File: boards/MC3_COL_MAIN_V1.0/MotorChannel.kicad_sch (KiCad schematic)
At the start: 7 parts, among them J7 MOTOR, U3 DRV8214RTER

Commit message: Schematic: local VM bulk per channel + LDO input filter
Two changes to isolate motor switching noise from the +3V3 rail.

1. MotorChannel.kicad_sch gains a 10 uF 0805 (C15850) from VM to GND beside
   the existing 1 uF. One symbol in the shared sheet, so five caps on the
   board. TI asks for 0.1 uF plus bulk at VM and the board bulk was over in
   the power block, at the far end of the VM trunk.

2. Power.kicad_sch gains FB4 + C32 on a new VM_LDO net between VM and the
   AMS1117's VI pin, plus a PWR_FLAG the new net needs for ERC. The regulator
   was a direct path from the motor rail to +3V3 - its PSRR is down to about
   30 dB by 100 kHz, well inside the PWM band.

FB4 is C14709 (Murata BLM18PG121SN1D, 120R@100MHz, 2 A, 50 mohm), NOT the 600R
C1002 used on VDDA and VCAN5 - that part is 200 mA / 450 mohm and would have
been marginal on current and cost ~110 mV of the AMS1117's dropout headroom.

Flagged in MIGRATION: FB4 with C32 forms an LC at roughly 115 kHz with Q ~2.8,
which could amplify rather than attenuate if the motor PWM lands near it. Needs
the firmware's PWM frequency to close, and damping (tantalum or an R leg) if it
does - shrinking C32 would make it worse, not better.

ERC: 0 errors, the same 8 intentional same_local_global warnings as before.

Co-Authored-By: Claude Opus 5 (1M context) <noreply@anthropic.com>
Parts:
- added C31: 10uF, MC3_COL_MAIN:C_0805_2012Metric, symbol Device:C
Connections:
- net GND: now also C31.2
- net VM: now also C31.1
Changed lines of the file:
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@@
 	(generator_version "10.0")
 	(paper "A4")
-	(text "Motor channel - one per leaf, instantiated x4. Implements: COL-COTS-0028 (DRV8214, integrated current sense + ripple counting) - vault Main-Board-01 Motor Channel. Layout: docs/design/parts/DRV8214.md. PAD + GND to the GND plane via thermal vias. VREF = +3V3 (TI typical app). PROVISIONAL: R_IPROPI, pull-ups."
-		(exclude_from_sim no)
-		(at 40 30 0)
-		(effects
-			(font
-				(size 1.5 1.5)
-			)
-		)
-	)
-	(text "Review 2026-08-22: R_IPROPI 6.8k -> hardware current trip 1.99 A (was 8.45k -> 1.60 A)."
-		(exclude_from_sim no)
-		(at 40 120 0)
-		(effects
-			(font
-				(size 1.5 1.5)
-			)
-		)
-	)
-	(text "A1/A0 tri-level address straps are set per instance on the root sheet (GND / +3V3)."
-		(exclude_from_sim no)
-		(at 40 115 0)
-		(effects
-			(font
-				(size 1.5 1.5)
-			)
-		)
-	)
 	(wire
 		(pts
-			(xy 87.63 82.55) (xy 85.09 82.55)
+			(xy 87.63 82.55)
+			(xy 85.09 82.55)
 		)
 		(stroke
@@
 	(wire
 		(pts
-			(xy 97.79 64.77) (xy 97.79 62.23)
+			(xy 97.79 64.77)
+			(xy 97.79 62.23)
 		)
 		(stroke
@@
 	(wire
 		(pts
-			(xy 87.63 80.01) (xy 85.09 80.01)
+			(xy 87.63 80.01)
+			(xy 85.09 80.01)
 		)
 		(stroke
@@
 	(wire
 		(pts
-			(xy 87.63 77.47) (xy 85.09 77.47)
+			(xy 87.63 77.47)
+			(xy 85.09 77.47)
 		)
 		(stroke
@@
 		)
 	)
+	(text "Motor channel - one per leaf, instantiated x4. Implements: COL-COTS-0028 (DRV8214, integrated current sense + ripple counting) - vault Main-Board-01 Motor Channel. Layout: docs/design/parts/DRV8214.md. PAD + GND to the GND plane via thermal vias. VREF = +3V3 (TI typical app). PROVISIONAL: R_IPROPI, pull-ups."
+		(at 40 30 0)
+		(effects
+			(font
+				(size 1.5 1.5)
+			)
+		)
+	)
+	(text "Review 2026-08-22: R_IPROPI 6.8k -> hardware current trip 1.99 A (was 8.45k -> 1.60 A)."
+		(at 40 120 0)
+		(effects
+			(font
+				(size 1.5 1.5)
+			)
+		)
+	)
+	(text "A1/A0 tri-level address straps are set per instance on the root sheet (GND / +3V3)."
+		(at 40 115 0)
+		(effects
+			(font
+				(size 1.5 1.5)
+			)
+		)
+	)
 	(label "+3V3"
 		(at 119.38 54.61 0)
@@
 	(label "+3V3"
 		(at 134.62 60.96 0)
+		(effects
+			(font
+				(size 1.27 1.27)
+			)
+			(justify left bottom)
+		)
+	)
+	(label "VM"
+		(at 90.17 54.61 0)
+		(effects
+			(font
+				(size 1.27 1.27)
+			)
+			(justify left bottom)
+		)
+	)
+	(label "GND"
+		(at 90.17 62.23 0)
 		(effects
 			(font
@@
 		(at 134.62 64.77 0)
 		(unit 1)
-		(body_style 1)
 		(exclude_from_sim no)
 		(in_bom yes)
 		(on_board yes)
-		(in_pos_files yes)
 		(dnp no)
 		(property "Reference" "R17"
@@
 			)
 		)
+		(body_style 1)
+		(in_pos_files yes)
 		(pin "1"
 		)
@@
 		(at 144.78 64.77 0)
 		(unit 1)
-		(body_style 1)
 		(exclude_from_sim no)
 		(in_bom yes)
 		(on_board yes)
-		(in_pos_files yes)
 		(dnp no)
 		(property "Reference" "R18"
@@
 			)
 		)
+		(body_style 1)
+		(in_pos_files yes)
 		(pin "1"
 		)
@@
 		(at 124.46 91.44 0)
 		(unit 1)
-		(body_style 1)
 		(exclude_from_sim no)
 		(in_bom yes)
 		(on_board yes)
-		(in_pos_files yes)
 		(dnp no)
 		(property "Reference" "R16"
@@
 			)
 		)
+		(body_style 1)
+		(in_pos_files yes)
 		(pin "2"
 		)
@@
 		(at 97.79 95.25 0)
 		(unit 1)
-		(body_style 1)
 		(exclude_from_sim no)
 		(in_bom yes)
 		(on_board yes)
-		(in_pos_files yes)
 		(dnp no)
 		(property "Reference" "#PWR011"
@@
 			)
 		)
+		(body_style 1)
+		(in_pos_files yes)
 		(pin "1"
 		)
@@
 		(at 80.01 58.42 0)
 		(unit 1)
-		(body_style 1)
 		(exclude_from_sim no)
 		(in_bom yes)
 		(on_board yes)
-		(in_pos_files yes)
 		(dnp no)
 		(property "Reference" "C18"
@@
 			)
 		)
+		(body_style 1)
+		(in_pos_files yes)
 		(pin "2"
 		)
@@
 		(at 100.33 80.01 0)
 		(unit 1)
-		(body_style 1)
 		(exclude_from_sim no)
 		(in_bom yes)
 		(on_board yes)
-		(in_pos_files yes)
 		(dnp no)
 		(property "Reference" "U3"
@@
 			)
 		)
+		(body_style 1)
+		(in_pos_files yes)
 		(pin "13"
 		)
@@
 		(at 149.86 95.25 0)
 		(unit 1)
-		(body_style 1)
 		(exclude_from_sim no)
 		(in_bom yes)
 		(on_board yes)
-		(in_pos_files yes)
 		(dnp no)
 		(property "Reference" "J7"
@@
 			)
 		)
+		(body_style 1)
+		(in_pos_files yes)
 		(pin "2"
 		)
@@
 		(at 102.87 64.77 0)
 		(unit 1)
-		(body_style 1)
 		(exclude_from_sim no)
 		(in_bom yes)
 		(on_board yes)
-		(in_pos_files yes)
 		(dnp no)
 		(property "Reference" "#PWR012"
@@
 			)
 		)
+		(body_style 1)
+		(in_pos_files yes)
 		(pin "1"
 		)
@@
 		(at 119.38 58.42 0)
 		(unit 1)
-		(body_style 1)
 		(exclude_from_sim no)
 		(in_bom yes)
 		(on_board yes)
-		(in_pos_files yes)
 		(dnp no)
 		(property "Reference" "C19"
@@
 			)
 		)
+		(body_style 1)
+		(in_pos_files yes)
 		(pin "1"
 		)
@@
 		)
 	)
+	(symbol
+		(lib_id "Device:C")
+		(at 90.17 58.42 0)
+		(unit 1)
+		(in_bom yes)
+		(on_board yes)
+		(dnp no)
+		(property "Reference" "C31"
+			(at 90.805 55.88 0)
+			(effects
+				(font
+					(size 1.27 1.27)
+				)
+				(justify left)
+			)
+		)
+		(property "Value" "10uF"
+			(at 90.805 60.96 0)
+			(effects
+				(font
+					(size 1.27 1.27)
+				)
+				(justify left)
+			)
+		)
+		(property "Footprint" "MC3_COL_MAIN:C_0805_2012Metric"
+			(at 90.17 58.42 0)
+			(hide yes)
+			(effects
+				(font
+					(size 1.27 1.27)
+				)
+			)
+		)
+		(property "Datasheet" ""
+			(at 90.17 58.42 0)
+			(hide yes)
+			(effects
+				(font
+					(size 1.27 1.27)
+				)
+			)
+		)
+		(instances
+			(project "MC3_COL_MAIN_V1.0"
+				(path "/7d5f4202-d55e-4c7b-a2df-dd599db38e48/5db6fbb9-0012-419b-b34a-9d86ac1f5217"
+					(reference "C31")
+					(unit 1)
+				)
+			)
+		)
+		(property "LCSC" "C15850"
+			(at 90.17 58.42 0)
+			(hide yes)
+			(effects
+				(font
+					(size 1.27 1.27)
+				)
+			)
+		)
+		(property "MPN" "CL21A106KAYNNNE"
+			(at 90.17 58.42 0)
+			(hide yes)
+			(effects
+				(font
+					(size 1.27 1.27)
+				)
+			)
+		)
+		(property "Note" "Local VM bulk, one per channel. Added 2026-08-22: TI SLVSH04 asks for 0.1uF + bulk at VM; the board bulk (C3/C4) is in the power block, so the five bridges' di/dt was being supplied through the VM trunk inductance. 25V X5R keeps most of its value at the 5V rail. PROVISIONAL - value not set by a vault CALC"
+			(at 90.17 58.42 0)
+			(hide yes)
+			(effects
+				(font
+					(size 1.27 1.27)
+				)
+			)
+		))
 )

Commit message: Schematic: new channel cap goes in as C? so annotation can assign per-instance refs
Adding it as C31 put that string in the symbol-level Reference property, so all
five sheet instances fell back to it and eeschema reported four duplicates.
Keep-existing annotation will not touch them because they do not look
unannotated. Reference is now C? on the property and on all five instance
paths; value, footprint, LCSC, MPN and the Note field are unchanged.

Co-Authored-By: Claude Opus 5 (1M context) <noreply@anthropic.com>
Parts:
- renumbered C31 to C?

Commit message: PCB: 8 new footprints from the schematic, fab attributes restored
Update PCB from Schematic applied: C31/C33/C34/C35/C36 (the per-channel VM
bulk, one per instance), C32 and FB4 (LDO input filter), plus JP1 - the solder
jumper the schematic still carries while the board uses R72. Net /Power/VM_LDO
created and U1 pin 3 reconnected to it. 101 -> 109 footprints.

That update strips fabrication attributes, because it syncs them from the
schematic symbol rather than the footprint library: J1 and J7-J11 dropped
exclude_from_pos_files/exclude_from_bom, and TP1-TP7 lost their attr line
entirely. Repaired with Update Footprints from Library scoped to all footprints
with only "reset fabrication attributes" ticked - the first attempt silently
covered just the 8 newly added parts because they were still selected.

Verified after: all 109 carry an attr line, J1/J7-J11 and TP1-TP7 are excluded
from BOM and position files again, and leaf3's hand-arranged silkscreen offsets
are untouched (the text reset box was deliberately left clear).

Still open: J12's library footprint (SolderPads_3x) never had the exclusions, so
the CAN pads remain in the BOM/PnP; JP1 needs resolving against R72; and the 8
new footprints are parked off-board awaiting placement.

Co-Authored-By: Claude Opus 5 (1M context) <noreply@anthropic.com>
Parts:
- gave numbers to parts that had none: 1
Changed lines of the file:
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@@
 		(in_pos_files yes)
 		(dnp no)
-		(property "Reference" "C?"
+		(property "Reference" "C31"
 			(at 90.805 55.88 0)
 			(show_name no)
@@
 			(project "MC3_COL_MAIN_V1.0"
 				(path "/7d5f4202-d55e-4c7b-a2df-dd599db38e48/5db6fbb9-0012-419b-b34a-9d86ac1f5217"
-					(reference "C?")
+					(reference "C33")
 					(unit 1)
 				)
 				(path "/7d5f4202-d55e-4c7b-a2df-dd599db38e48/8cfd3b4a-99dc-4b05-a7ad-f8199ec40931"
-					(reference "C?")
+					(reference "C36")
 					(unit 1)
 				)
 				(path "/7d5f4202-d55e-4c7b-a2df-dd599db38e48/9d20a086-3ce1-4783-a1c3-78685ff35655"
-					(reference "C?")
+					(reference "C35")
 					(unit 1)
 				)
 				(path "/7d5f4202-d55e-4c7b-a2df-dd599db38e48/a93ffbcb-09b2-46f4-87ff-b0a1b53638e4"
-					(reference "C?")
+					(reference "C31")
 					(unit 1)
 				)
 				(path "/7d5f4202-d55e-4c7b-a2df-dd599db38e48/f0c3363d-cc6b-4f74-be1d-ed0c2c093cdf"
-					(reference "C?")
+					(reference "C34")
 					(unit 1)
 				)

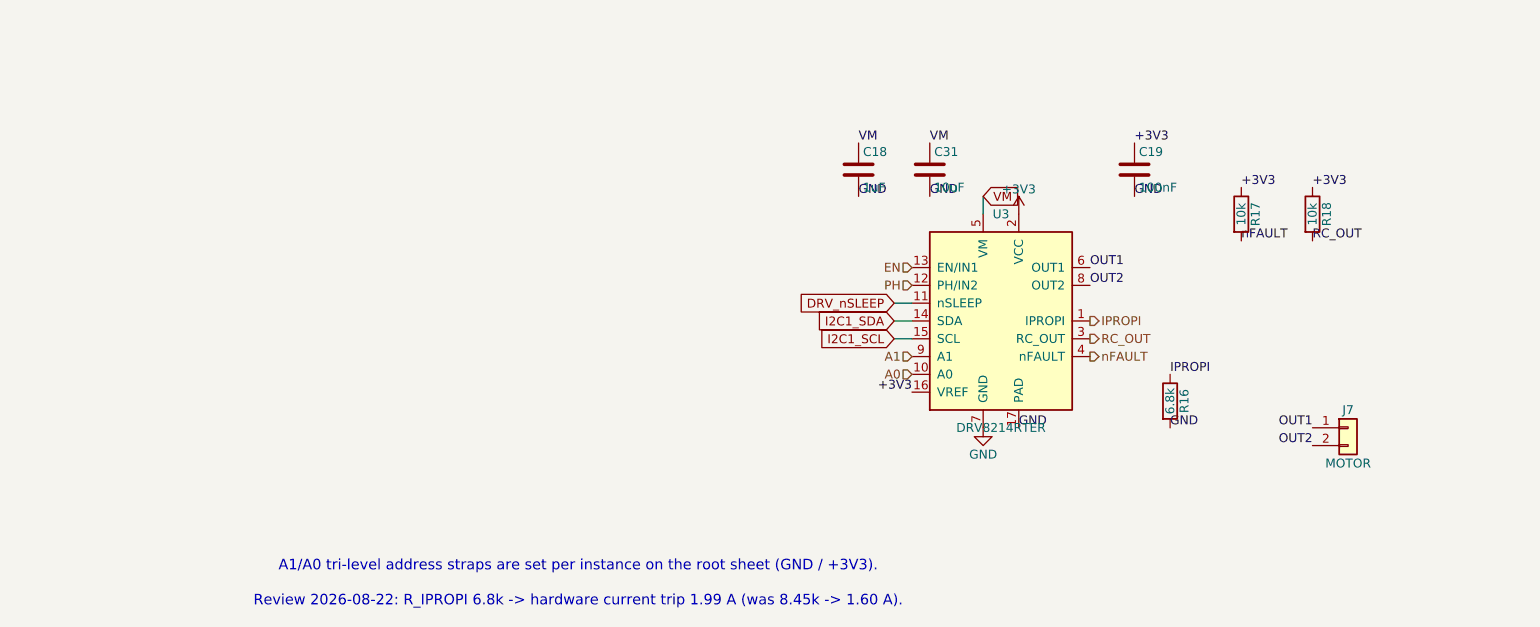
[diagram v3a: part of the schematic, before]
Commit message: WIP before MCU pin remap: board state, vault sync, GND vias placed
Co-Authored-By: Claude Fable 5 <noreply@anthropic.com>
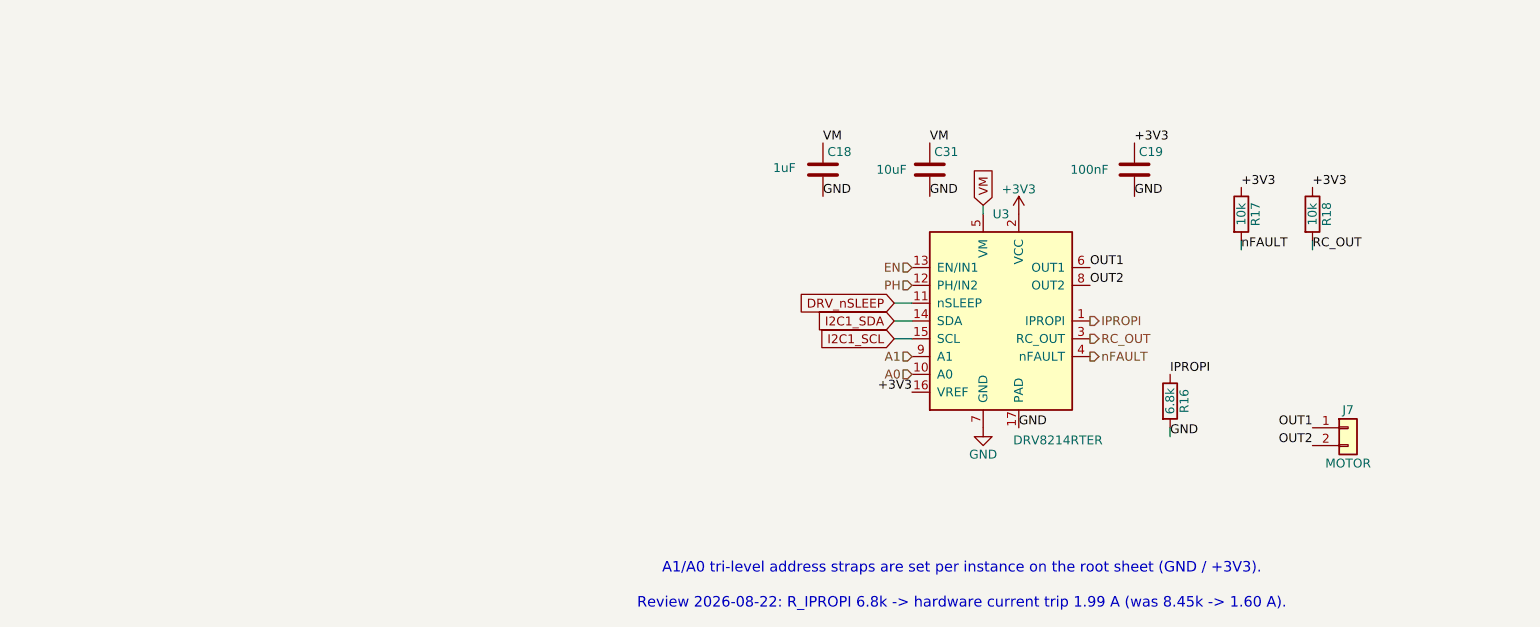
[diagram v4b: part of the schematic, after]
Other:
- moved on the sheet: C18
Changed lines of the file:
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@@
 	(text "Review 2026-08-22: R_IPROPI 6.8k -> hardware current trip 1.99 A (was 8.45k -> 1.60 A)."
 		(exclude_from_sim no)
-		(at 40 120 0)
+		(at 94.742 120.316 0)
 		(effects
 			(font
@@
 	(text "A1/A0 tri-level address straps are set per instance on the root sheet (GND / +3V3)."
 		(exclude_from_sim no)
-		(at 40 115 0)
+		(at 94.742 115.316 0)
 		(effects
 			(font
@@
 	(wire
 		(pts
-			(xy 97.79 64.77) (xy 97.79 62.23)
+			(xy 97.79 64.77) (xy 97.79 63.5)
 		)
 		(stroke
@@
 	(wire
 		(pts
-			(xy 87.63 77.47) (xy 85.09 77.47)
+			(xy 144.78 69.85) (xy 144.78 68.58)
 		)
 		(stroke
@@
 		)
 	)
+	(wire
+		(pts
+			(xy 134.62 69.85) (xy 134.62 68.58)
+		)
+		(stroke
+			(width 0)
+			(type default)
+		)
+	)
+	(wire
+		(pts
+			(xy 87.63 77.47) (xy 85.09 77.47)
+		)
+		(stroke
+			(width 0)
+			(type default)
+		)
+	)
+	(wire
+		(pts
+			(xy 124.46 96.52) (xy 124.46 95.25)
+		)
+		(stroke
+			(width 0)
+			(type default)
+		)
+	)
 	(label "+3V3"
 		(at 119.38 54.61 0)
@@
 	)
 	(label "VM"
-		(at 80.01 54.61 0)
+		(at 74.93 54.61 0)
 		(effects
 			(font
@@
 	)
 	(label "GND"
-		(at 80.01 62.23 0)
+		(at 74.93 62.23 0)
 		(effects
 			(font
@@
 	)
 	(label "nFAULT"
-		(at 134.62 68.58 0)
+		(at 134.62 69.85 0)
 		(effects
 			(font
@@
 	)
 	(label "GND"
-		(at 124.46 95.25 0)
+		(at 124.46 96.52 0)
 		(effects
 			(font
@@
 	)
 	(label "RC_OUT"
-		(at 144.78 68.58 0)
+		(at 144.78 69.85 0)
 		(effects
 			(font
@@
 	(global_label "VM"
 		(shape input)
-		(at 97.79 62.23 0)
+		(at 97.79 63.5 90)
 		(effects
 			(font
@@
 		)
 		(property "Intersheetrefs" "${INTERSHEET_REFS}"
-			(at 97.79 62.23 0)
+			(at 97.79 63.5 90)
 			(hide yes)
 			(show_name no)
@@
 	(symbol
 		(lib_id "Device:C")
-		(at 80.01 58.42 0)
+		(at 74.93 58.42 0)
 		(unit 1)
 		(body_style 1)
@@
 		(dnp no)
 		(property "Reference" "C18"
-			(at 80.645 55.88 0)
+			(at 75.565 55.88 0)
 			(show_name no)
 			(do_not_autoplace no)
@@
 		)
 		(property "Value" "1uF"
-			(at 80.645 60.96 0)
+			(at 67.818 58.166 0)
 			(show_name no)
 			(do_not_autoplace no)
@@
 		)
 		(property "Footprint" "MC3_COL_MAIN:C_0603_1608Metric"
-			(at 80.01 58.42 0)
+			(at 74.93 58.42 0)
 			(hide yes)
 			(show_name no)
@@
 		)
 		(property "Datasheet" ""
-			(at 80.01 58.42 0)
+			(at 74.93 58.42 0)
 			(hide yes)
 			(show_name no)
@@
 		)
 		(property "Description" ""
-			(at 80.01 58.42 0)
+			(at 74.93 58.42 0)
 			(show_name no)
 			(do_not_autoplace no)
@@
 		)
 		(property "Note" "VM bypass 1uF X5R/X7R >=10V - vault Main-Board-01 BOM (driver decoupling)"
-			(at 80.01 58.42 0)
+			(at 74.93 58.42 0)
 			(hide yes)
 			(show_name no)
@@
 		)
 		(property "LCSC" "C15849"
-			(at 80.01 58.42 0)
+			(at 74.93 58.42 0)
 			(hide yes)
 			(show_name no)
@@
 		)
 		(property "MPN" "CL10A105KB8NNNC"
-			(at 80.01 58.42 0)
+			(at 74.93 58.42 0)
 			(hide yes)
 			(show_name no)
@@
 		)
 		(property "Value" "10uF"
-			(at 90.805 60.96 0)
+			(at 82.55 58.42 0)
 			(show_name no)
 			(do_not_autoplace no)
@@
 		)
 		(property "Value" "DRV8214RTER"
-			(at 100.33 95.25 0)
+			(at 108.458 97.028 0)
 			(show_name no)
 			(do_not_autoplace no)
@@
 		)
 		(property "Value" "100nF"
-			(at 120.015 60.96 0)
-			(show_name no)
-			(do_not_autoplace no)
+			(at 110.236 58.42 0)
+			(show_name no)
+			(do_not_autoplace no)
